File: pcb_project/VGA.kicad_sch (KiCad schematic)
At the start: 0 parts

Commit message: Add VGA with 4bit DAC
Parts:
- added J1: DE15_Socket_HighDensity_MountingHoles, symbol Connector:DE15_Socket_HighDensity_MountingHoles
- added R13, R14, R15, R16, R21, R23, R25, R27, R29, R31, R33, R35: 540, symbol Device:R
- added R17, R18, R19, R20, R22, R24, R26, R28, R30, R32, R34, R36: 270, symbol Device:R
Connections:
- new net: R30.2, R31.1, R32.1
- new net: R32.2, R33.1, R34.1
- new net: R16.1, R19.2, R20.1
- new net: R14.1, R17.2, R18.1
- new net: R24.2, R25.1, R26.1
- new net: R26.2, R27.1, R28.1
- new net: R34.2, R35.1, R36.1
- new net: R22.2, R23.1, R24.1
- new net: R15.1, R18.2, R19.1
- new net B0: R35.2
- new net B1: R33.2
- new net B2: R31.2
- new net B3: R29.2
- new net BGND: J1.8
- new net BLUE_75Ohm: J1.3, R29.1, R30.1
- new net Empty: J1.9
- new net G0: R27.2
- new net G1: R25.2
- new net G2: R23.2
- new net G3: R21.2
- new net GGND: J1.7
- new net GND: J1.5, R20.2, R28.2, R36.2
- new net GREEN_75Ohm: J1.2, R21.1, R22.1
- new net HSYNC: J1.13
- new net ID0: J1.11
- new net ID1: J1.12
- new net ID2: J1.4
- new net ID3: J1.15
- new net R0: R16.2
- new net R1: R15.2
- new net R2: R14.2
- new net R3: R13.2
- new net RED_75Ohm: J1.1, R13.1, R17.1
- new net RGND: J1.6
- new net SGND: J1.10
- new net VSYNC: J1.14

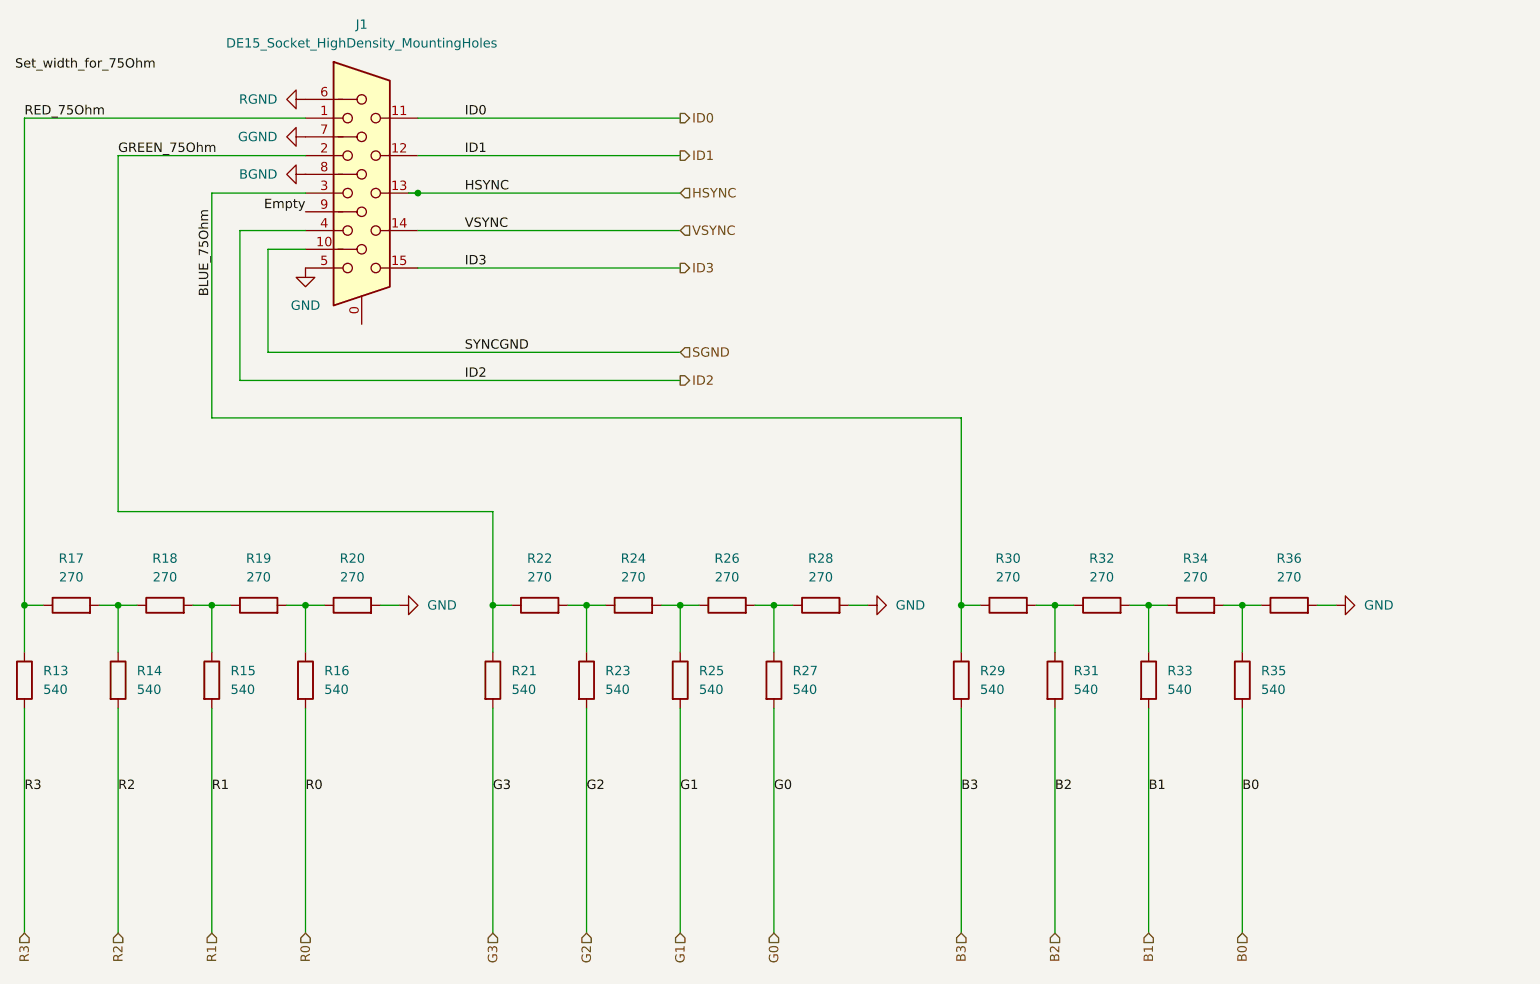
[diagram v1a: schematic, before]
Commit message: 16bit binary weighted dac, FPGA power
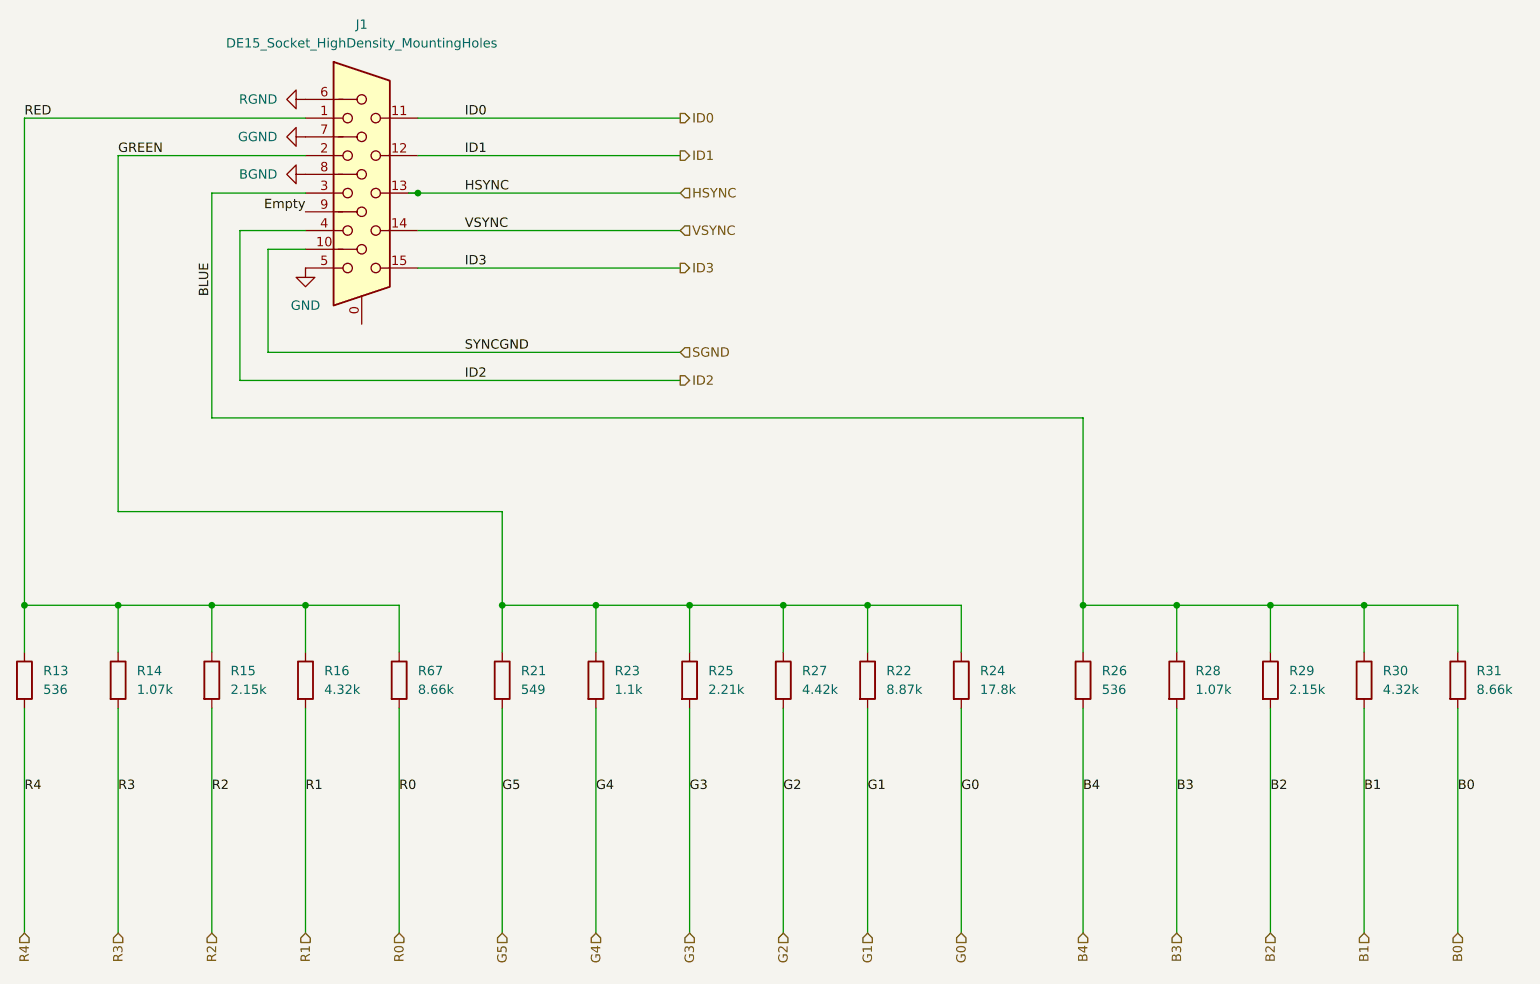
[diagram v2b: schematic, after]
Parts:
- removed R17, R18, R19, R20, R32, R34, R36: 270, symbol Device:R
- removed R33, R35: 540, symbol Device:R
- added R67: 8.66k, symbol Device:R
- R13: value 540 -> 536
- R14: value 540 -> 1.07k
- R15, R29: value 540 -> 2.15k
- R16: value 540 -> 4.32k
- R21: value 540 -> 549
- R22: value 270 -> 8.87k
- R23: value 540 -> 1.1k
- R24: value 270 -> 17.8k
- R25: value 540 -> 2.21k
- R26: value 270 -> 536
- R27: value 540 -> 4.42k
- R28: value 270 -> 1.07k
- R30: value 270 -> 4.32k
- R31: value 540 -> 8.66k
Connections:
- net BLUE_75Ohm is gone; now on net BLUE: J1.3, R29.1, R30.1
- net GREEN_75Ohm is gone; now on net GREEN: J1.2, R21.1, R22.1
- net RED_75Ohm is gone; now on net RED: J1.1, R13.1
- net B0: now also R31.2
- net B1: now also R30.2
- net B2: now also R29.2; no longer R31.2
- net B3: now also R28.2; no longer R29.2
- net G0: now also R24.2; no longer R27.2
- net G1: now also R22.2; no longer R25.2
- net G2: now also R27.2; no longer R23.2
- net G3: now also R25.2; no longer R21.2
- net GND: no longer R28.2
- net R0: now also R67.2; no longer R16.2
- net R1: now also R16.2; no longer R15.2
- net R2: now also R15.2; no longer R14.2
- net R3: now also R14.2; no longer R13.2
- net BLUE: now reaches R31.1
- net BLUE: now also R26.1, R28.1; no longer R30.2
- net RED: now reaches R16.1
- net RED: now also R14.1, R15.1, R67.1
- net GREEN: now reaches R23.1, R24.1
- net GREEN: now also R25.1, R27.1; no longer R22.2
- new net B4: R26.2
- new net G4: R23.2
- new net G5: R21.2
- new net R4: R13.2
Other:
- moved on the sheet: R21, R23, R25, R27

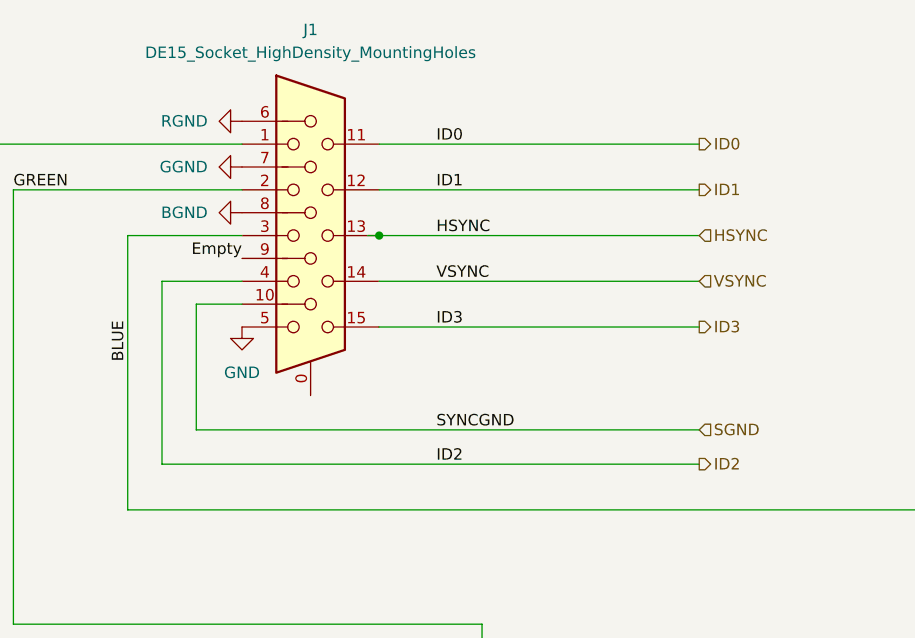
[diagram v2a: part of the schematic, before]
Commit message: VGA Root + Change FPGA Oscilator to 3.3v
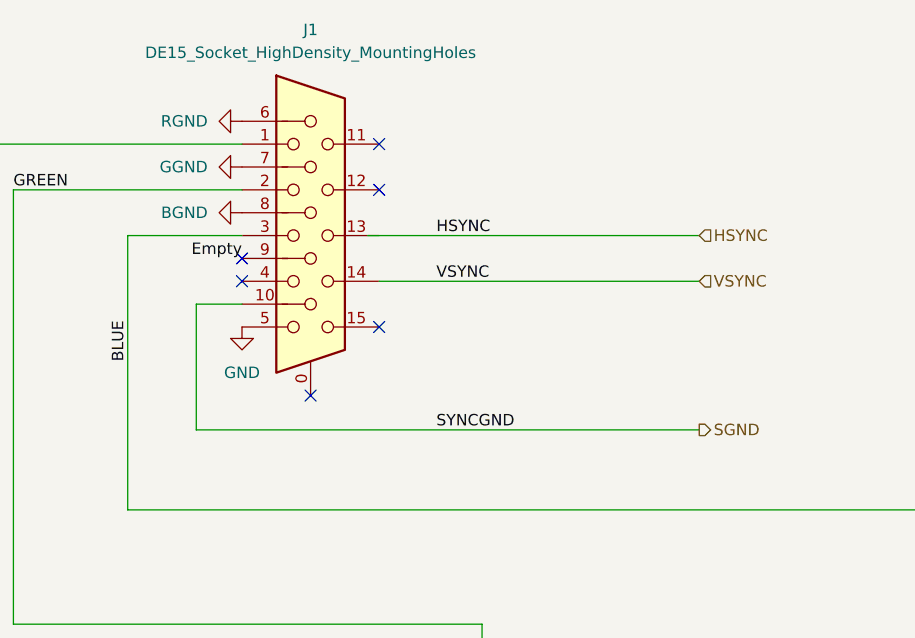
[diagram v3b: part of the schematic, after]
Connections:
- net HSYNC: no longer J1.13
- net ID0: no longer names the net of J1.11
- net ID1: no longer names the net of J1.12
- net ID2: no longer names the net of J1.4
- net ID3: no longer names the net of J1.15
- no-connect marks 0 -> 6
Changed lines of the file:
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@@
-	)
-	(junction
-		(at 91.44 45.72)
-		(diameter 0)
-		(color 0 0 0 0)
 	)
 	(junction
@@
 		(color 0 0 0 0)
 	)
-	(wire
-		(pts
-			(xy 90.17 45.72) (xy 91.44 45.72)
-		)
-		(stroke
-			(width 0)
-			(type default)
-		)
+	(no_connect
+		(at 91.44 40.64)
+	)
+	(no_connect
+		(at 91.44 35.56)
+	)
+	(no_connect
+		(at 76.2 50.8)
+	)
+	(no_connect
+		(at 91.44 55.88)
+	)
+	(no_connect
+		(at 76.2 48.26)
+	)
+	(no_connect
+		(at 83.82 63.5)
 	)
 	(wire
@@
 	(wire
 		(pts
-			(xy 67.31 50.8) (xy 67.31 71.12)
-		)
-		(stroke
-			(width 0)
-			(type default)
-		)
-	)
-	(wire
-		(pts
 			(xy 63.5 115.57) (xy 63.5 146.05)
 		)
@@
 	(wire
 		(pts
-			(xy 91.44 40.64) (xy 127 40.64)
-		)
-		(stroke
-			(width 0)
-			(type default)
-		)
-	)
-	(wire
-		(pts
 			(xy 88.9 107.95) (xy 88.9 101.6)
 		)
@@
 	(wire
 		(pts
-			(xy 91.44 45.72) (xy 127 45.72)
+			(xy 90.17 45.72) (xy 127 45.72)
 		)
 		(stroke
@@
 	(wire
 		(pts
-			(xy 91.44 35.56) (xy 127 35.56)
-		)
-		(stroke
-			(width 0)
-			(type default)
-		)
-	)
-	(wire
-		(pts
 			(xy 76.2 53.34) (xy 71.12 53.34)
 		)
@@
 	(wire
 		(pts
-			(xy 91.44 55.88) (xy 127 55.88)
-		)
-		(stroke
-			(width 0)
-			(type default)
-		)
-	)
-	(wire
-		(pts
 			(xy 207.01 101.6) (xy 207.01 107.95)
 		)
@@
 	(wire
 		(pts
-			(xy 67.31 71.12) (xy 127 71.12)
-		)
-		(stroke
-			(width 0)
-			(type default)
-		)
-	)
-	(wire
-		(pts
 			(xy 71.12 53.34) (xy 71.12 67.31)
 		)
@@
 		(pts
 			(xy 128.27 101.6) (xy 128.27 107.95)
-		)
-		(stroke
-			(width 0)
-			(type default)
-		)
-	)
-	(wire
-		(pts
-			(xy 76.2 50.8) (xy 67.31 50.8)
 		)
 		(stroke
@@
 		)
 	)
-	(label "ID0"
-		(at 97.79 35.56 0)
-		(effects
-			(font
-				(size 1.27 1.27)
-			)
-			(justify left bottom)
-		)
-	)
 	(label "R4"
 		(at 38.1 127 0)
@@
 		)
 	)
-	(label "ID2"
-		(at 97.79 71.12 0)
-		(effects
-			(font
-				(size 1.27 1.27)
-			)
-			(justify left bottom)
-		)
-	)
 	(label "R3"
 		(at 50.8 127 0)
@@
 		)
 	)
-	(label "ID1"
-		(at 97.79 40.64 0)
-		(effects
-			(font
-				(size 1.27 1.27)
-			)
-			(justify left bottom)
-		)
-	)
 	(label "R1"
 		(at 76.2 127 0)
@@
 		)
 	)
-	(label "ID3"
-		(at 97.79 55.88 0)
-		(effects
-			(font
-				(size 1.27 1.27)
-			)
-			(justify left bottom)
-		)
-	)
 	(label "VSYNC"
 		(at 97.79 50.8 0)
@@
 		)
 	)
-	(hierarchical_label "ID0"
+	(hierarchical_label "R3"
+		(shape input)
+		(at 50.8 146.05 270)
+		(effects
+			(font
+				(size 1.27 1.27)
+			)
+			(justify right)
+		)
+	)
+	(hierarchical_label "G4"
+		(shape input)
+		(at 115.57 146.05 270)
+		(effects
+			(font
+				(size 1.27 1.27)
+			)
+			(justify right)
+		)
+	)
+	(hierarchical_label "B4"
+		(shape input)
+		(at 181.61 146.05 270)
+		(effects
+			(font
+				(size 1.27 1.27)
+			)
+			(justify right)
+		)
+	)
+	(hierarchical_label "G3"
+		(shape input)
+		(at 128.27 146.05 270)
+		(effects
+			(font
+				(size 1.27 1.27)
+			)
+			(justify right)
+		)
+	)
+	(hierarchical_label "R1"
+		(shape input)
+		(at 76.2 146.05 270)
+		(effects
+			(font
+				(size 1.27 1.27)
+			)
+			(justify right)
+		)
+	)
+	(hierarchical_label "B3"
+		(shape input)
+		(at 194.31 146.05 270)
+		(effects
+			(font
+				(size 1.27 1.27)
+			)
+			(justify right)
+		)
+	)
+	(hierarchical_label "B1"
+		(shape input)
+		(at 219.71 146.05 270)
+		(effects
+			(font
+				(size 1.27 1.27)
+			)
+			(justify right)
+		)
+	)
+	(hierarchical_label "R0"
+		(shape input)
+		(at 88.9 146.05 270)
+		(effects
+			(font
+				(size 1.27 1.27)
+			)
+			(justify right)
+		)
+	)
+	(hierarchical_label "G2"
+		(shape input)
+		(at 140.97 146.05 270)
+		(effects
+			(font
+				(size 1.27 1.27)
+			)
+			(justify right)
+		)
+	)
+	(hierarchical_label "B0"
+		(shape input)
+		(at 232.41 146.05 270)
+		(effects
+			(font
+				(size 1.27 1.27)
+			)
+			(justify right)
+		)
+	)
+	(hierarchical_label "G5"
+		(shape input)
+		(at 102.87 146.05 270)
+		(effects
+			(font
+				(size 1.27 1.27)
+			)
+			(justify right)
+		)
+	)
+	(hierarchical_label "G1"
+		(shape input)
+		(at 152.4 146.05 270)
+		(effects
+			(font
+				(size 1.27 1.27)
+			)
+			(justify right)
+		)
+	)
+	(hierarchical_label "SGND"
 		(shape output)
-		(at 127 35.56 0)
-		(effects
-			(font
-				(size 1.27 1.27)
-			)
-			(justify left)
-		)
-	)
-	(hierarchical_label "R3"
-		(shape input)
-		(at 50.8 146.05 270)
-		(effects
-			(font
-				(size 1.27 1.27)
-			)
-			(justify right)
-		)
-	)
-	(hierarchical_label "G4"
-		(shape input)
-		(at 115.57 146.05 270)
-		(effects
-			(font
-				(size 1.27 1.27)
-			)
-			(justify right)
-		)
-	)
-	(hierarchical_label "ID3"
-		(shape output)
-		(at 127 55.88 0)
-		(effects
-			(font
-				(size 1.27 1.27)
-			)
-			(justify left)
-		)
-	)
-	(hierarchical_label "B4"
-		(shape input)
-		(at 181.61 146.05 270)
-		(effects
-			(font
-				(size 1.27 1.27)
-			)
-			(justify right)
-		)
-	)
-	(hierarchical_label "G3"
-		(shape input)
-		(at 128.27 146.05 270)
-		(effects
-			(font
-				(size 1.27 1.27)
-			)
-			(justify right)
-		)
-	)
-	(hierarchical_label "R1"
-		(shape input)
-		(at 76.2 146.05 270)
-		(effects
-			(font
-				(size 1.27 1.27)
-			)
-			(justify right)
-		)
-	)
-	(hierarchical_label "ID2"
-		(shape output)
-		(at 127 71.12 0)
-		(effects
-			(font
-				(size 1.27 1.27)
-			)
-			(justify left)
-		)
-	)
-	(hierarchical_label "B3"
-		(shape input)
-		(at 194.31 146.05 270)
-		(effects
-			(font
-				(size 1.27 1.27)
-			)
-			(justify right)
-		)
-	)
-	(hierarchical_label "B1"
-		(shape input)
-		(at 219.71 146.05 270)
-		(effects
-			(font
-				(size 1.27 1.27)
-			)
-			(justify right)
-		)
-	)
-	(hierarchical_label "R0"
-		(shape input)
-		(at 88.9 146.05 270)
-		(effects
-			(font
-				(size 1.27 1.27)
-			)
-			(justify right)
-		)
-	)
-	(hierarchical_label "ID1"
-		(shape output)
-		(at 127 40.64 0)
-		(effects
-			(font
-				(size 1.27 1.27)
-			)
-			(justify left)
-		)
-	)
-	(hierarchical_label "G2"
-		(shape input)
-		(at 140.97 146.05 270)
-		(effects
-			(font
-				(size 1.27 1.27)
-			)
-			(justify right)
-		)
-	)
-	(hierarchical_label "B0"
-		(shape input)
-		(at 232.41 146.05 270)
-		(effects
-			(font
-				(size 1.27 1.27)
-			)
-			(justify right)
-		)
-	)
-	(hierarchical_label "G5"
-		(shape input)
-		(at 102.87 146.05 270)
-		(effects
-			(font
-				(size 1.27 1.27)
-			)
-			(justify right)
-		)
-	)
-	(hierarchical_label "G1"
-		(shape input)
-		(at 152.4 146.05 270)
-		(effects
-			(font
-				(size 1.27 1.27)
-			)
-			(justify right)
-		)
-	)
-	(hierarchical_label "SGND"
-		(shape input)
 		(at 127 67.31 0)
 		(effects
